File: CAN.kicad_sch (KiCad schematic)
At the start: 6 parts, among them U12 SIT1051TK/3, U13 ZX-SH1.0-4PWT

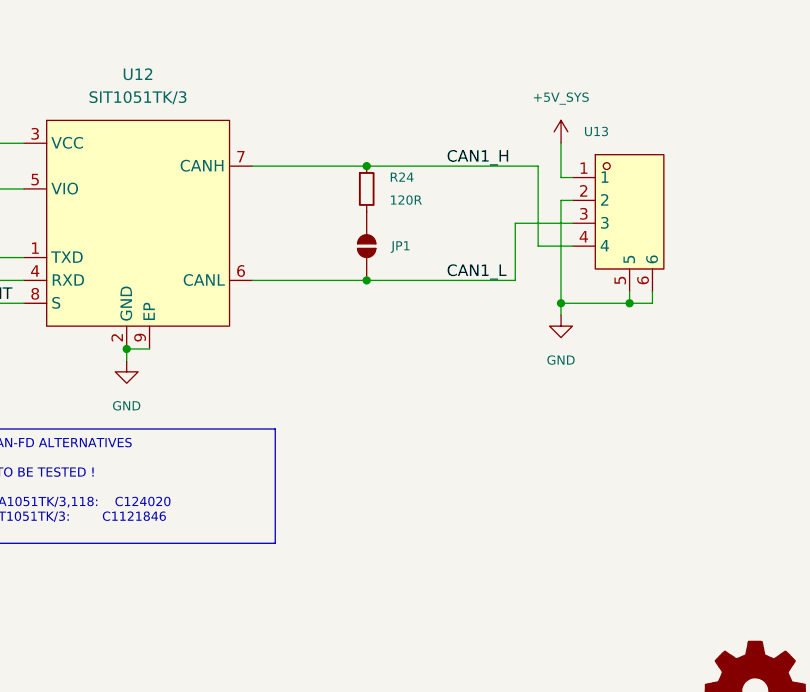
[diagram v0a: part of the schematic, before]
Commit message: new PCB custom outline
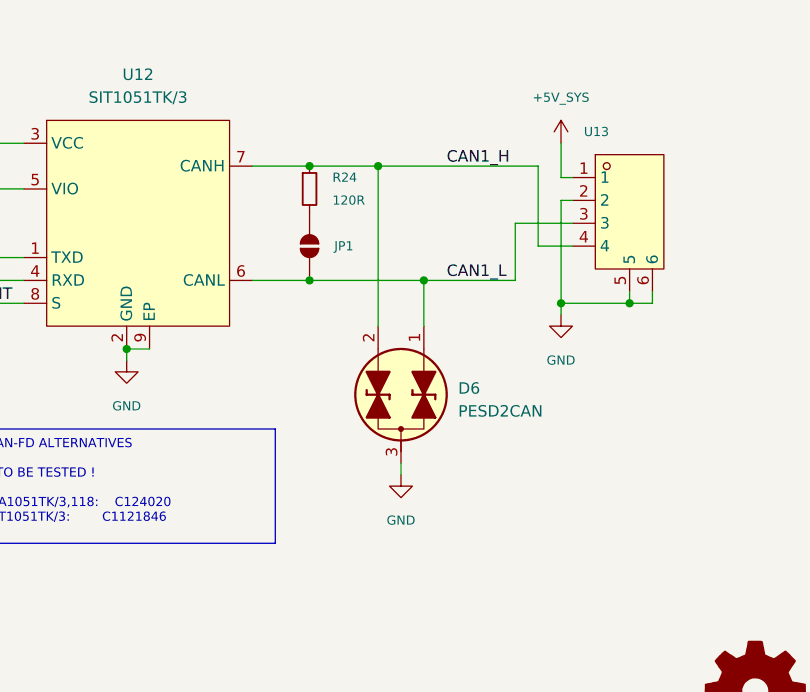
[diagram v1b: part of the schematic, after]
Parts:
- added D6: PESD2CAN, PCM_Package_TO_SOT_SMD_AKL:SOT-23, symbol PCM_Diode_TVS_AKL:PESD2CAN
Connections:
- net CAN1_H: now also D6.2 (A2)
- net CAN1_L: now also D6.1 (A1)
- net GND: now also D6.3 (Com)
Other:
- moved on the sheet: JP1, R24
